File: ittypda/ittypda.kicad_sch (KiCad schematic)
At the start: 148 parts, among them CN1 S2B-PH-SM4-TB, J1 USB_C_Receptacle_USB2.0_14P, J2 Conn_01x04_Pin, SW1 Switch, SW10 Switch, SW11 Switch, SW12 Switch, SW13 Switch, SW14 Switch, SW15 Switch, SW16 Switch, SW17 Switch, SW18 Switch, SW19 Switch, SW2 Switch, SW20 Switch, SW21 Switch, SW22 Switch, SW23 Switch, SW24 Switch, SW26 Switch, SW27 Switch, SW28 Switch, SW29 Switch, SW3 Switch, SW30 Switch, SW31 Switch, SW32 Switch, SW33 Switch, SW34 Switch, SW36 Switch, SW37 Switch, SW38 Switch, SW39 Switch, SW4 Switch, SW41 Switch, SW42 Switch, SW43 Switch, SW44 Switch, SW45 Switch, SW46 Switch, SW47 Switch, SW48 Switch, SW49 Switch, SW5 Switch, SW50 Switch, SW51 Switch, SW52 Switch, SW53 Switch, SW54 Switch, SW55 Switch, SW56 Switch, SW57 Switch, SW58 Switch, SW59 Switch, SW6 Switch, SW60 Switch, SW61 Switch, SW62 SW_SPDT, SW7 Switch, SW8 Switch, SW9 Switch, U1 STM32F401RETx, U2 BQ24040DSQR, U3 TLV75801PDRV, Y1 16Mhz

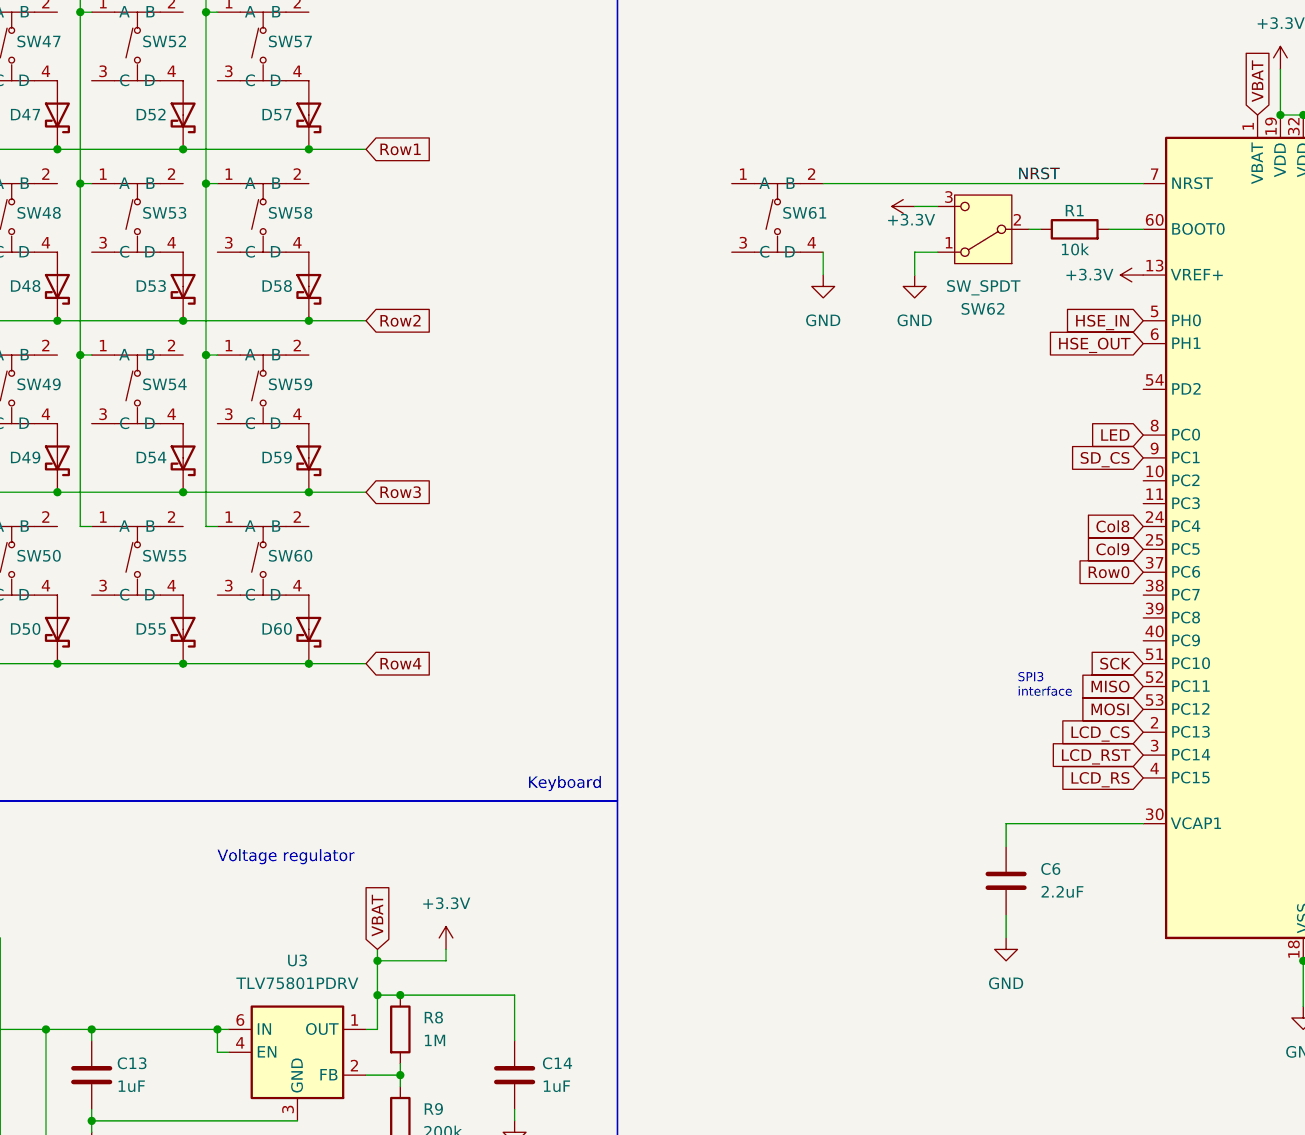
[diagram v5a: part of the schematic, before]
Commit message: add a power slide switch that cuts off 3v3 and also removed the NRST switch
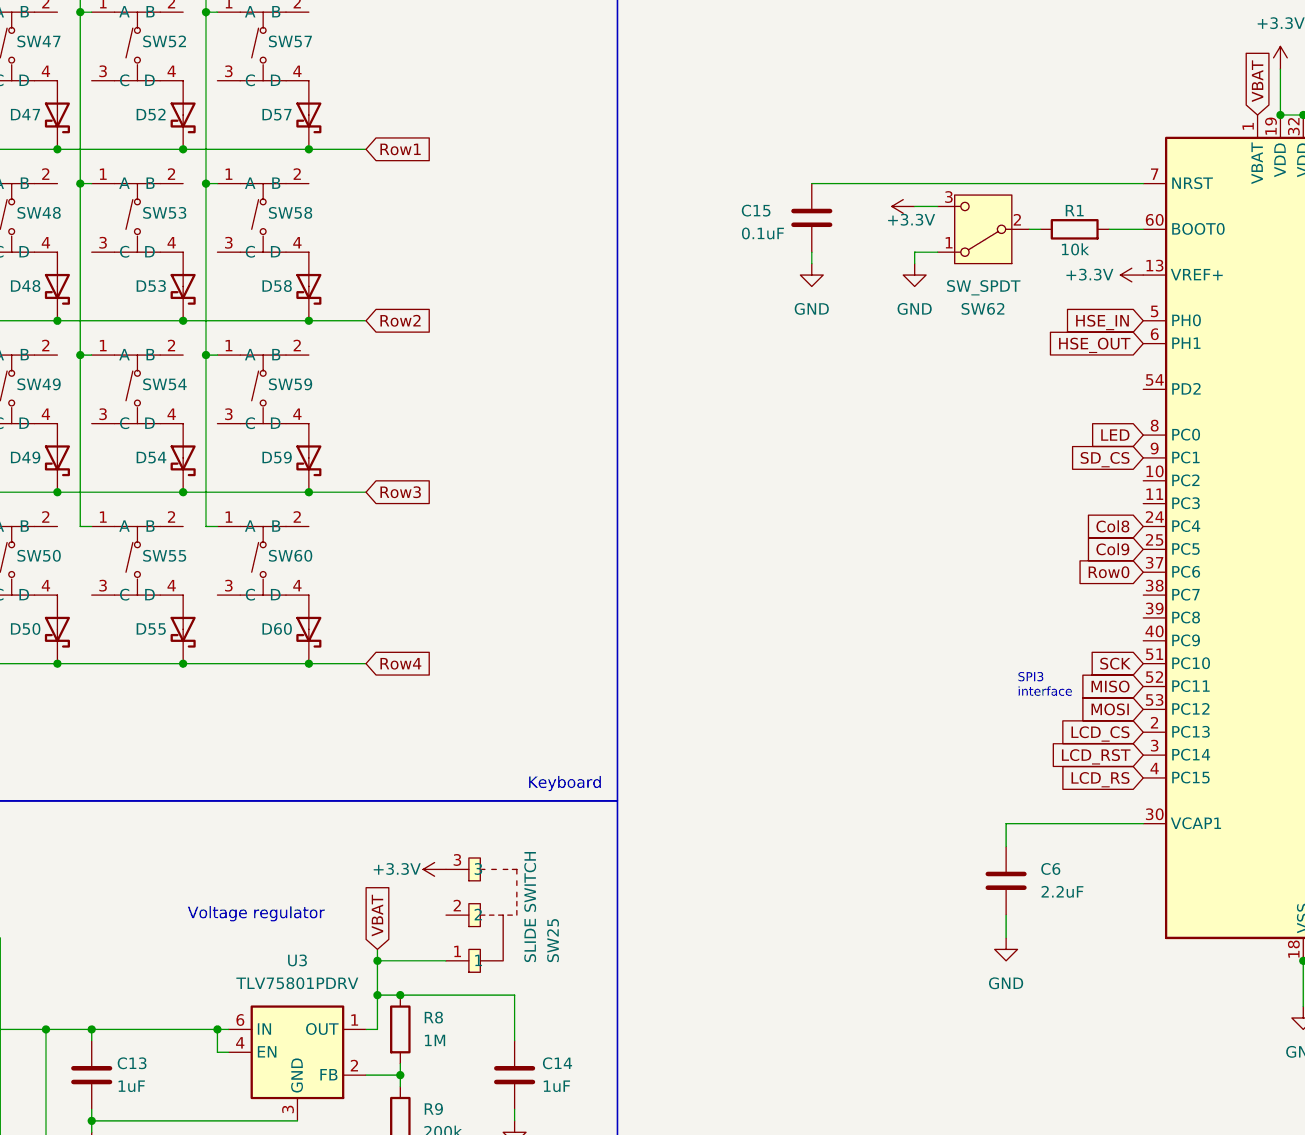
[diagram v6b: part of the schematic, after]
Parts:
- removed SW61: Switch, easyeda2kicad:SW-SMD_4P-L5.1-W5.1-P3.70-LS6.5-TL_H1.5, symbol easyeda2kicad:TS-1187A-B-A-B
- added C15: 0.1uF, symbol Device:C
- added SW25: SLIDE SWITCH, easyeda2kicad:SW-SMD_3P-L9.1-W3.5-P2.50_MST-12D18G2, symbol easyeda2kicad:MST-12D18G2SMDSLIDESWITCH
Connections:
- net +3.3V: now also SW25.3; no longer C14.1, R8.1, U1.1 (VBAT), U3.1 (OUT)
- net GND: now also C15.2
- net NRST: no longer names the net of U1.7 (NRST)
- net NRST: now also C15.1
- new net VBAT: C14.1, R8.1, SW25.1, U1.1 (VBAT), U3.1 (OUT)

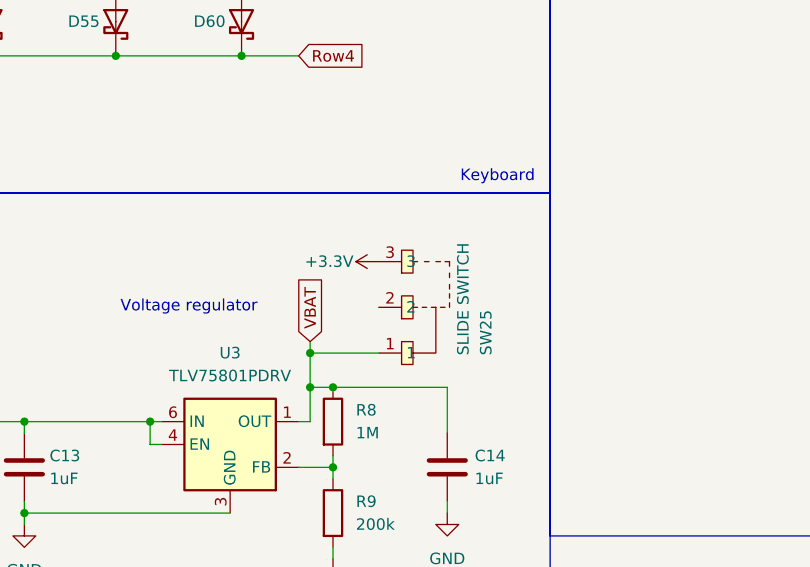
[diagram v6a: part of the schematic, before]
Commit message: fix slide switch
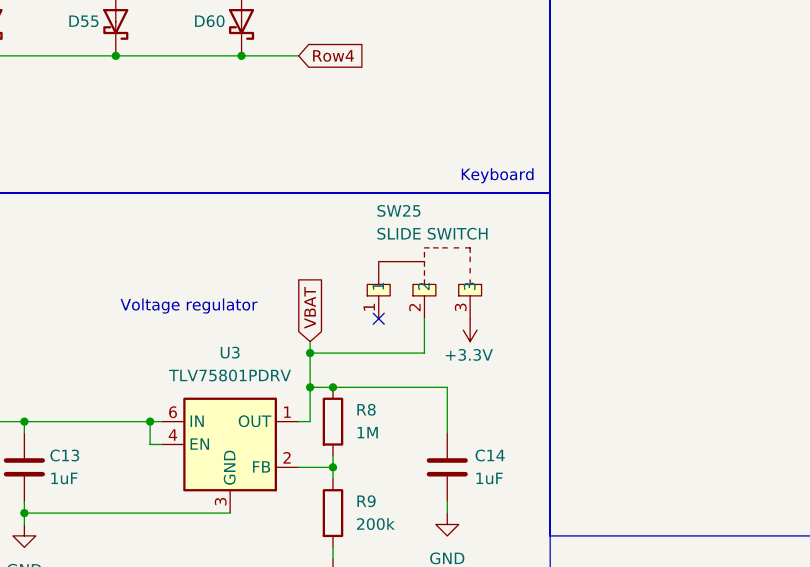
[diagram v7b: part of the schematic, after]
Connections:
- net VBAT: now also SW25.2; no longer SW25.1
- no-connect marks 8 -> 9
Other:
- moved on the sheet: SW25
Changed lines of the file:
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@@
 	)
 	(no_connect
+		(at 217.17 166.37)
+	)
+	(no_connect
 		(at 48.26 261.62)
 	)
@@
 	(wire
 		(pts
-			(xy 217.17 170.18) (xy 209.55 170.18)
+			(xy 209.55 170.18) (xy 222.25 170.18)
 		)
 		(stroke
@@
 	(wire
 		(pts
+			(xy 222.25 170.18) (xy 222.25 166.37)
+		)
+		(stroke
+			(width 0)
+			(type default)
+		)
+	)
+	(wire
+		(pts
 			(xy 162.56 83.82) (xy 162.56 102.87)
 		)
@@
 	(symbol
 		(lib_id "easyeda2kicad:MST-12D18G2SMDSLIDESWITCH")
-		(at 220.98 166.37 90)
+		(at 220.98 162.56 0)
+		(mirror x)
 		(unit 1)
 		(body_style 1)
@@
 		(dnp no)
 		(property "Reference" "SW25"
-			(at 229.108 170.434 0)
+			(at 216.916 154.432 0)
 			(show_name no)
 			(do_not_autoplace no)
@@
 		)
 		(property "Value" "SLIDE SWITCH"
-			(at 226.568 170.434 0)
+			(at 216.916 156.972 0)
 			(show_name no)
 			(do_not_autoplace no)
@@
 		)
 		(property "Footprint" "easyeda2kicad:SW-SMD_3P-L9.1-W3.5-P2.50_MST-12D18G2"
-			(at 224.79 166.37 0)
+			(at 220.98 158.75 0)
 			(hide yes)
 			(show_name no)
@@
 		)
 		(property "Datasheet" "https://www.lcsc.com/datasheet/C49023765.pdf"
-			(at 227.33 166.37 0)
+			(at 220.98 156.21 0)
 			(hide yes)
 			(show_name no)
@@
 		)
 		(property "Description" ""
-			(at 220.98 166.37 0)
+			(at 220.98 162.56 0)
 			(hide yes)
 			(show_name no)
@@
 		)
 		(property "Manufacturer" "SHOU HAN(首韩)"
-			(at 229.87 166.37 0)
+			(at 220.98 153.67 0)
 			(hide yes)
 			(show_name no)
@@
 		)
 		(property "MPN" "MST-12D18G2 SMD Slide Switch"
-			(at 232.41 166.37 0)
+			(at 220.98 151.13 0)
 			(hide yes)
 			(show_name no)
@@
 		)
 		(property "LCSC Part" "C49023765"
-			(at 234.95 166.37 0)
+			(at 220.98 148.59 0)
 			(hide yes)
 			(show_name no)
@@
 	(symbol
 		(lib_id "power:+3.3V")
-		(at 217.17 160.02 90)
+		(at 227.33 166.37 180)
 		(unit 1)
 		(body_style 1)
@@
 		(dnp no)
 		(property "Reference" "#PWR021"
-			(at 220.98 160.02 0)
+			(at 227.33 162.56 0)
 			(hide yes)
 			(show_name no)
@@
 		)
 		(property "Value" "+3.3V"
-			(at 214.376 160.02 90)
+			(at 229.87 170.434 0)
 			(show_name no)
 			(do_not_autoplace no)
@@
 		)
 		(property "Footprint" ""
-			(at 217.17 160.02 0)
+			(at 227.33 166.37 0)
 			(hide yes)
 			(show_name no)
@@
 		)
 		(property "Datasheet" ""
-			(at 217.17 160.02 0)
+			(at 227.33 166.37 0)
 			(hide yes)
 			(show_name no)
@@
 		)
 		(property "Description" "Power symbol creates a global label with name \"+3.3V\""
-			(at 217.17 160.02 0)
+			(at 227.33 166.37 0)
 			(hide yes)
 			(show_name no)

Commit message: use bigger footprint for slide switch
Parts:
- SW25: footprint easyeda2kicad:SW-SMD_3P-L9.1-W3.5-P2.50_MST-12D18G2 -> easyeda2kicad:SW-SMD_MST-12D18G4-SPDT-SLIDE-SWITCH; LCSC Part C49023765 -> C49023767
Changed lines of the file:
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@@
 			)
 		)
-		(property "Footprint" "easyeda2kicad:SW-SMD_3P-L9.1-W3.5-P2.50_MST-12D18G2"
+		(property "Footprint" "easyeda2kicad:SW-SMD_MST-12D18G4-SPDT-SLIDE-SWITCH"
 			(at 220.98 158.75 0)
 			(hide yes)
@@
 			)
 		)
-		(property "LCSC Part" "C49023765"
+		(property "LCSC Part" "C49023767"
 			(at 220.98 148.59 0)
 			(hide yes)
